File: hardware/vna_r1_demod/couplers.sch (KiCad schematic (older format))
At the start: 0 parts

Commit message: work on vna r1 demod schematic
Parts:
- added C? (x2): C_Small, symbol C_Small
- added R? (x2): R_Small, symbol R_Small
- added TP?: TP_RF, symbol TP_RF
- added U? (x2): resistive_bridge, symbol resistive_bridge
- added U? (x2): CONN_SMA_2GND, symbol CONN_SMA_2GND
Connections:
- new net GND: U?.4 (GND), U?.4 (GND)
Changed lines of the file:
@@
 $Descr A4 11693 8268
 encoding utf-8
-Sheet 1 4
+Sheet 5 6
 Title ""
 Date ""
@@
 Comment4 ""
 $EndDescr
+$Comp
+L resistive_bridge U?
+U 1 1 5AC73B65
+P 5150 4500
+F 0 "U?" H 4450 4900 60  0000 C CNN
+F 1 "resistive_bridge" H 4700 5000 60  0000 C CNN
+F 2 "" H 5450 4500 60  0001 C CNN
+F 3 "" H 5450 4500 60  0001 C CNN
+	1    5150 4500
+	1    0    0    -1
+$EndComp
+$Comp
+L resistive_bridge U?
+U 1 1 5AC73B7B
+P 7550 4500
+F 0 "U?" H 6850 4900 60  0000 C CNN
+F 1 "resistive_bridge" H 7100 5000 60  0000 C CNN
+F 2 "" H 7850 4500 60  0001 C CNN
+F 3 "" H 7850 4500 60  0001 C CNN
+	1    7550 4500
+	1    0    0    -1
+$EndComp
+$Comp
+L CONN_SMA_2GND U?
+U 1 1 5AC73BCD
+P 3000 4450
+F 0 "U?" H 2700 4650 60  0000 C CNN
+F 1 "CONN_SMA_2GND" H 3050 4750 60  0000 C CNN
+F 2 "" H 3000 4450 60  0000 C CNN
+F 3 "" H 3000 4450 60  0000 C CNN
+	1    3000 4450
+	1    0    0    -1
+$EndComp
+$Comp
+L CONN_SMA_2GND U?
+U 1 1 5AC73C3F
+P 9800 4450
+F 0 "U?" H 9500 4650 60  0000 C CNN
+F 1 "CONN_SMA_2GND" H 9850 4750 60  0000 C CNN
+F 2 "" H 9800 4450 60  0000 C CNN
+F 3 "" H 9800 4450 60  0000 C CNN
+	1    9800 4450
+	-1   0    0    -1
+$EndComp
+$Comp
+L R_Small R?
+U 1 1 5AC73CAD
+P 5100 3550
+F 0 "R?" H 5130 3570 50  0000 L CNN
+F 1 "R_Small" H 5130 3510 50  0000 L CNN
+F 2 "" H 5100 3550 50  0001 C CNN
+F 3 "" H 5100 3550 50  0001 C CNN
+	1    5100 3550
+	1    0    0    -1
+$EndComp
+$Comp
+L R_Small R?
+U 1 1 5AC73D0D
+P 7550 3500
+F 0 "R?" H 7580 3520 50  0000 L CNN
+F 1 "R_Small" H 7580 3460 50  0000 L CNN
+F 2 "" H 7550 3500 50  0001 C CNN
+F 3 "" H 7550 3500 50  0001 C CNN
+	1    7550 3500
+	1    0    0    -1
+$EndComp
+Text HLabel 5100 3050 1    60   Output ~ 0
+CPL_FWD
+Text HLabel 7900 3100 1    60   Output ~ 0
+CPL_REV
+$Comp
+L TP_RF TP?
+U 1 1 5AC74090
+P 6350 5000
+F 0 "TP?" V 6150 5150 60  0000 C CNN
+F 1 "TP_RF" V 6150 4900 60  0001 C CNN
+F 2 "" H 6350 5100 60  0001 C CNN
+F 3 "" H 6350 5100 60  0001 C CNN
+	1    6350 5000
+	1    0    0    -1
+$EndComp
+$Comp
+L GND #PWR?
+U 1 1 5AC74432
+P 5150 5050
+F 0 "#PWR?" H 5150 4800 50  0001 C CNN
+F 1 "GND" H 5150 4900 50  0000 C CNN
+F 2 "" H 5150 5050 50  0001 C CNN
+F 3 "" H 5150 5050 50  0001 C CNN
+	1    5150 5050
+	1    0    0    -1
+$EndComp
+Wire Wire Line
+	5150 4950 5150 5050
+$Comp
+L GND #PWR?
+U 1 1 5AC74470
+P 7550 5050
+F 0 "#PWR?" H 7550 4800 50  0001 C CNN
+F 1 "GND" H 7550 4900 50  0000 C CNN
+F 2 "" H 7550 5050 50  0001 C CNN
+F 3 "" H 7550 5050 50  0001 C CNN
+	1    7550 5050
+	1    0    0    -1
+$EndComp
+Wire Wire Line
+	7550 5050 7550 4950
+$Comp
+L C_Small C?
+U 1 1 5AC74707
+P 8900 4500
+F 0 "C?" H 8910 4570 50  0000 L CNN
+F 1 "C_Small" H 8910 4420 50  0000 L CNN
+F 2 "" H 8900 4500 50  0001 C CNN
+F 3 "" H 8900 4500 50  0001 C CNN
+	1    8900 4500
+	0    -1   -1   0
+$EndComp
+$Comp
+L C_Small C?
+U 1 1 5AC748D3
+P 3850 4500
+F 0 "C?" H 3860 4570 50  0000 L CNN
+F 1 "C_Small" H 3860 4420 50  0000 L CNN
+F 2 "" H 3850 4500 50  0001 C CNN
+F 3 "" H 3850 4500 50  0001 C CNN
+	1    3850 4500
+	0    -1   -1   0
+$EndComp
 $EndSCHEMATC

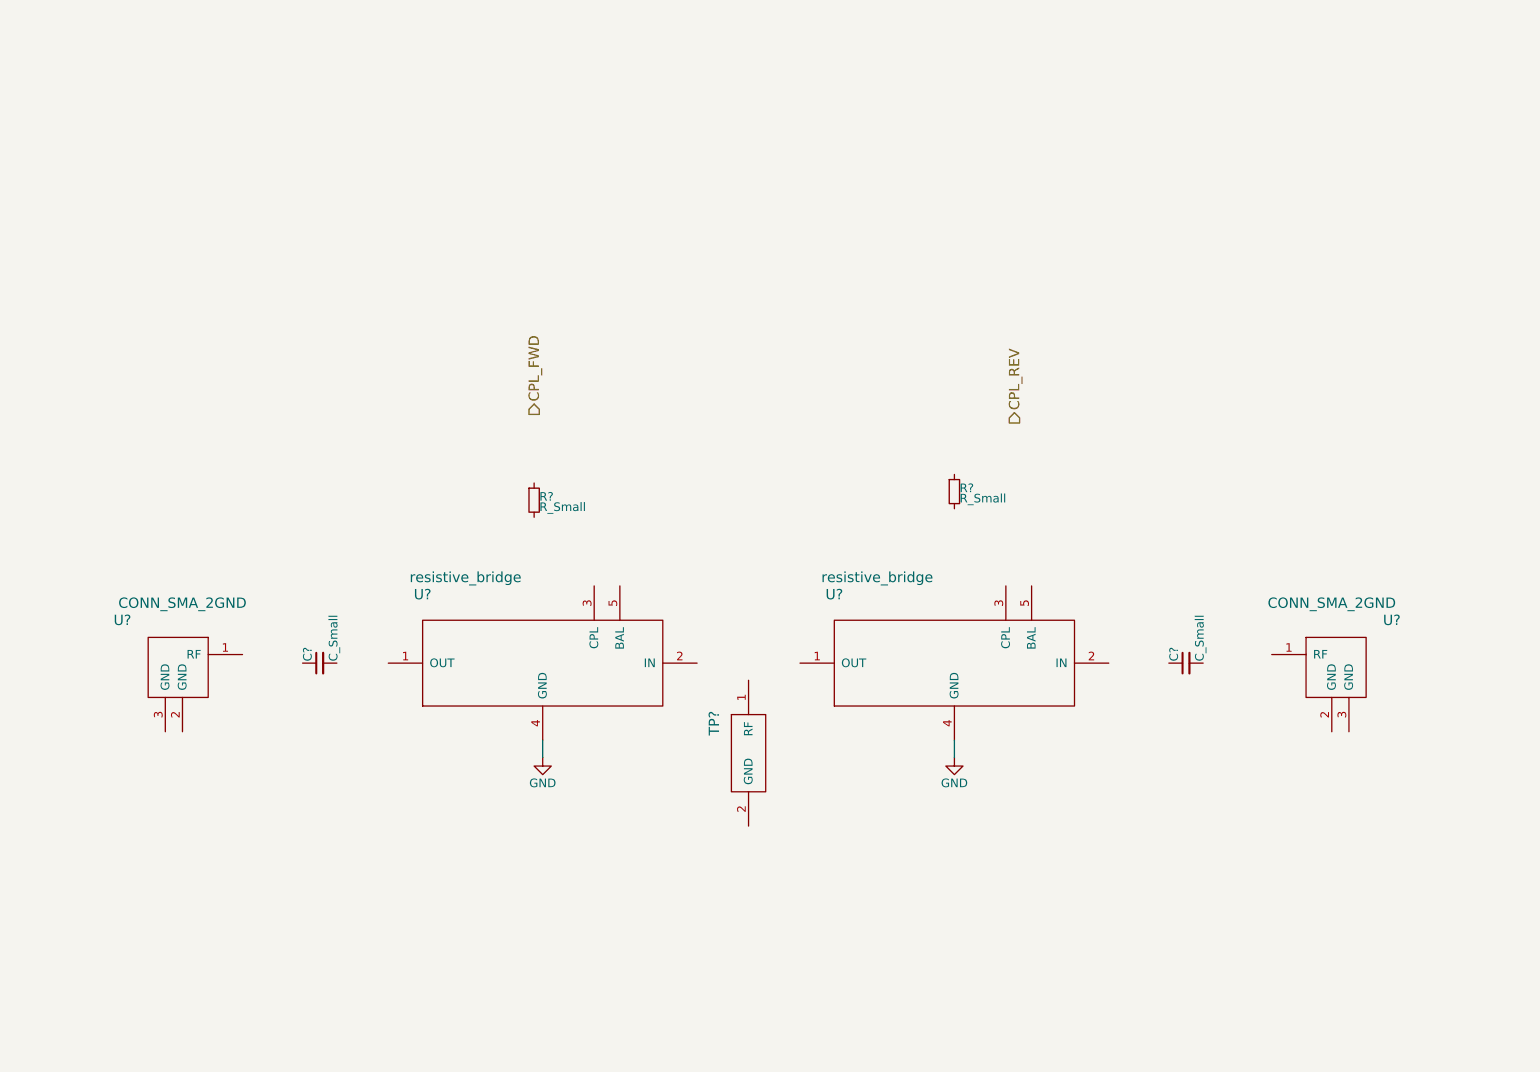
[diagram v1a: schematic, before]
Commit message: ethernet and usb layout on vna control board..
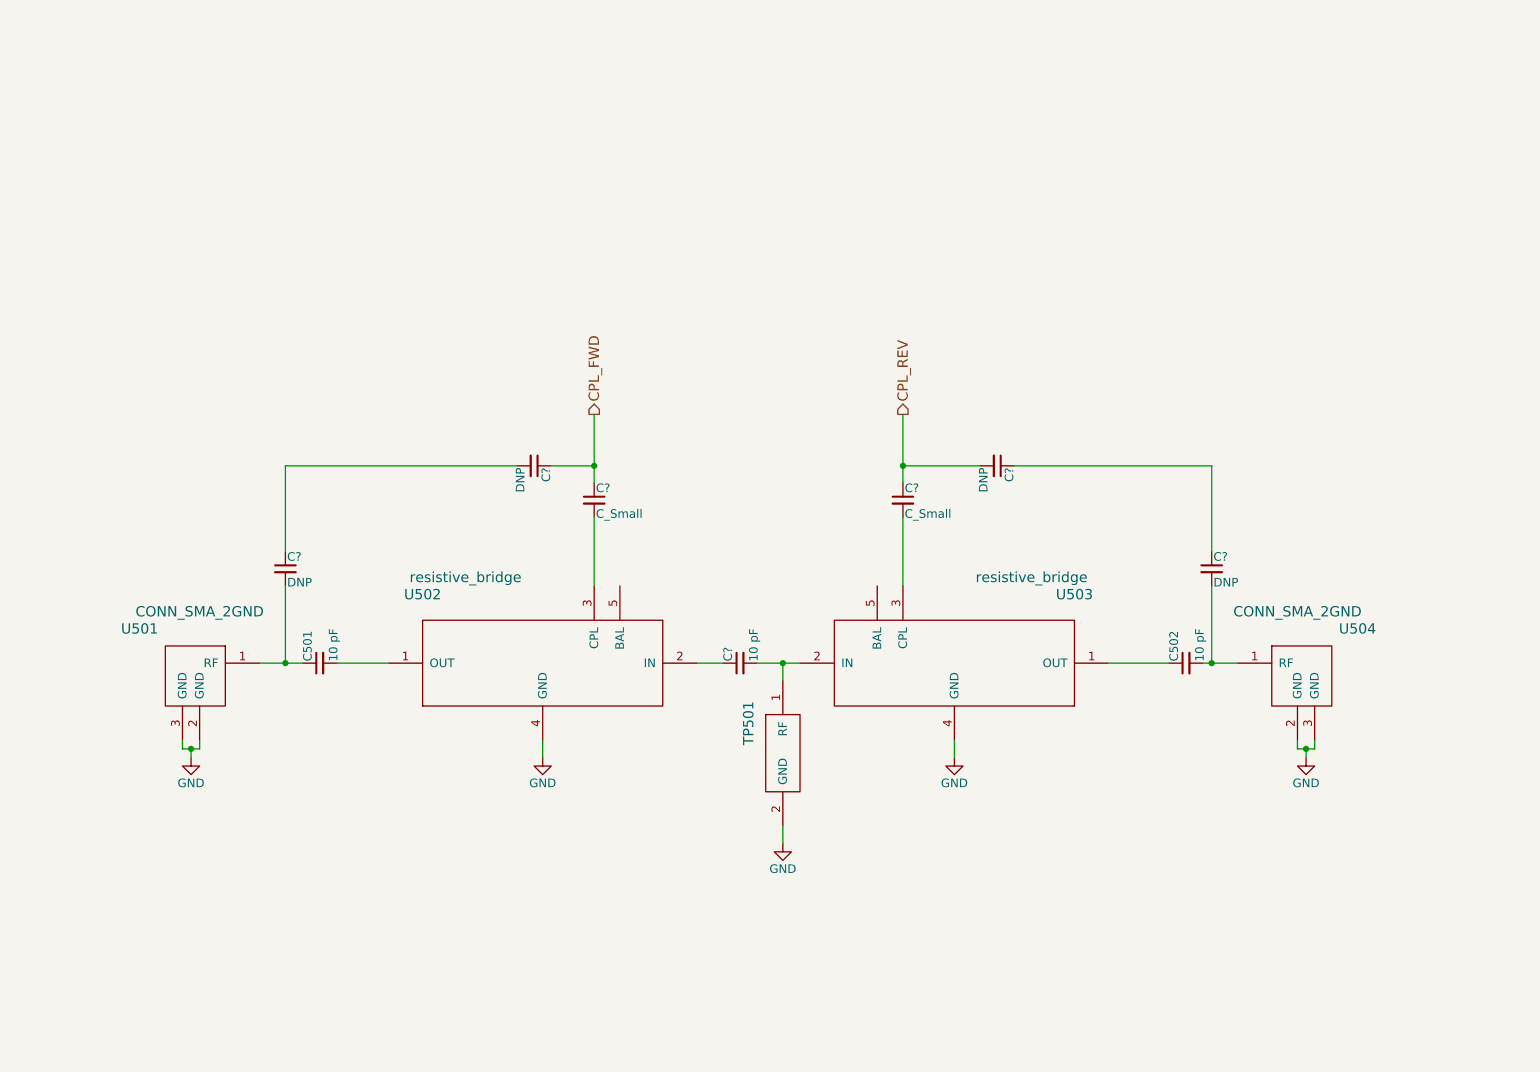
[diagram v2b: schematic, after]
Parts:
- removed R? (x2): R_Small, symbol R_Small
- added C?: 10 pF, symbol C_Small
- added C? (x4): DNP, symbol C_Small
- added C? (x2): C_Small, symbol C_Small
- C501, C502: renamed from C?; value C_Small -> 10 pF
- TP501: renamed from TP?; footprint (none) -> vna_footprints:TP-P20B
- U501, U504: renamed from U?; footprint (none) -> vna_footprints:SMA_901-10512_6p7MIL_FR408_CPW_LAUNCH
- U502, U503: renamed from U?; footprint (none) -> vna_footprints:resistive_bridge_osh_fr408_ustrip
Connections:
- net CPL_FWD: now also C?.1, C?.1
- net CPL_REV: now also C?.1, C?.2
- net GND: now also TP501.2 (GND), U501.2 (GND), U501.3 (GND), U504.2 (GND), U504.3 (GND)
- net at U502.1 (OUT): now also C501.2
- net at U502.2 (IN): now also C?.1
- net at U502.3 (CPL): now also C?.2
- net at U503.1 (OUT): now also C502.1
- net at U503.2 (IN): now also TP501.1 (RF), C?.2
- net at U503.3 (CPL): now also C?.2
- net at U501.1 (RF): now also C501.1, C?.2
- net at U504.1 (RF): now also C502.2, C?.2
- new net: C?.1, C?.2
- new net: C?.1, C?.1
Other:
- moved on the sheet: TP501, U501, U504

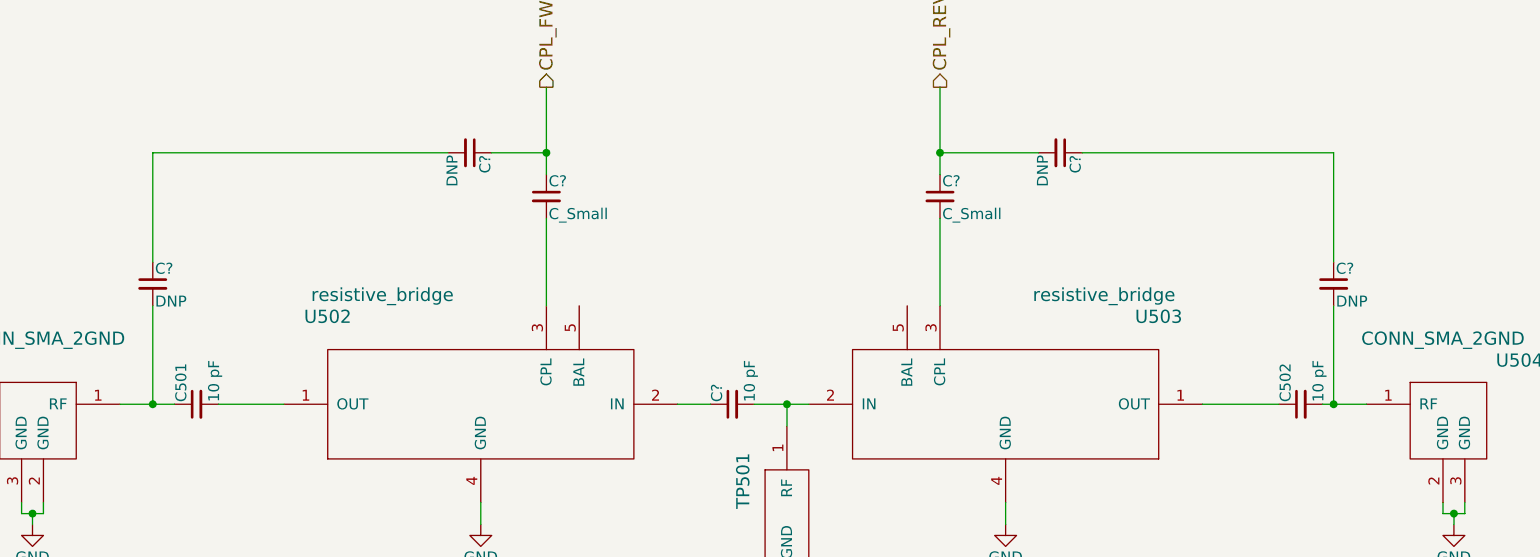
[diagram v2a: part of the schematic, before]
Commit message: footprint assignment for vna r1 synth and demod
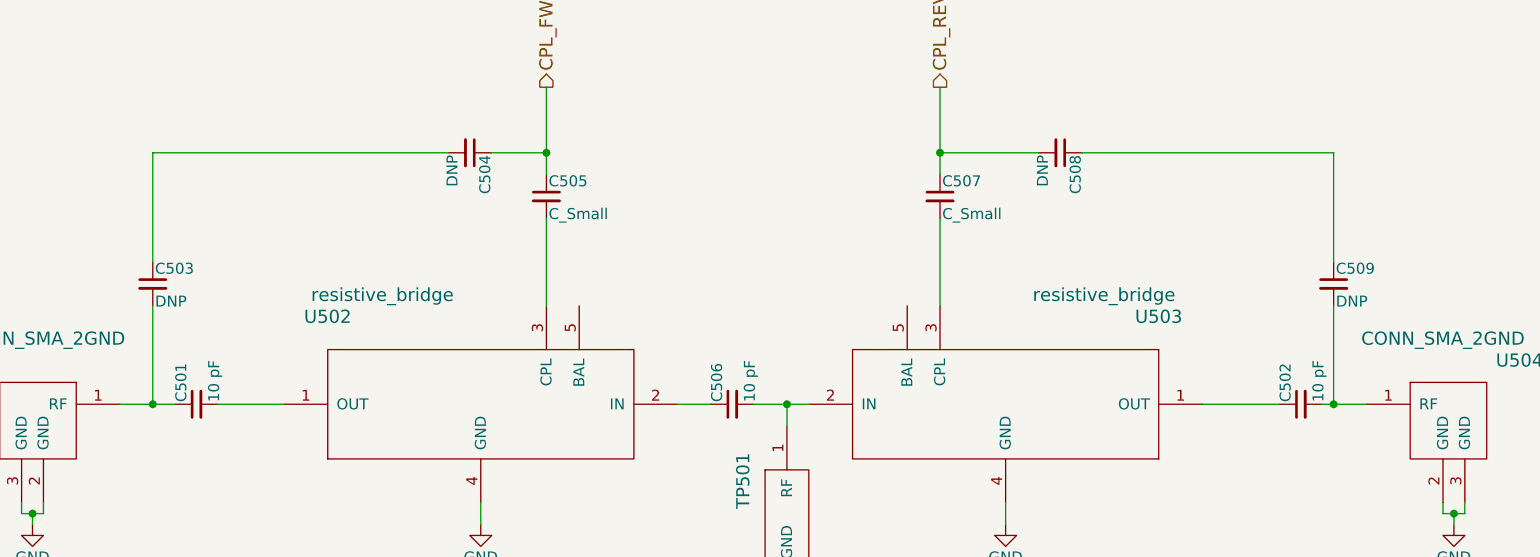
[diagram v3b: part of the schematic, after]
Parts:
- C501, C502: footprint (none) -> Capacitors_SMD:C_0201
- C503, C504, C505, C506, C507, C508, C509: renamed from C?; footprint (none) -> Capacitors_SMD:C_0201
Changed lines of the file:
@@
 $EndComp
 $Comp
-L GND #PWR070
+L GND #PWR502
 U 1 1 5AC74432
 P 5150 5050
-F 0 "#PWR070" H 5150 4800 50  0001 C CNN
+F 0 "#PWR502" H 5150 4800 50  0001 C CNN
 F 1 "GND" H 5150 4900 50  0000 C CNN
 F 2 "" H 5150 5050 50  0001 C CNN
@@
 $EndComp
 $Comp
-L GND #PWR071
+L GND #PWR504
 U 1 1 5AC74470
 P 7550 5050
-F 0 "#PWR071" H 7550 4800 50  0001 C CNN
+F 0 "#PWR504" H 7550 4800 50  0001 C CNN
 F 1 "GND" H 7550 4900 50  0000 C CNN
 F 2 "" H 7550 5050 50  0001 C CNN
@@
 F 0 "C502" H 8910 4570 50  0000 L CNN
 F 1 "10 pF" H 8910 4420 50  0000 L CNN
-F 2 "" H 8900 4500 50  0001 C CNN
+F 2 "Capacitors_SMD:C_0201" H 8900 4500 50  0001 C CNN
 F 3 "" H 8900 4500 50  0001 C CNN
 	1    8900 4500
@@
 F 0 "C501" H 3860 4570 50  0000 L CNN
 F 1 "10 pF" H 3860 4420 50  0000 L CNN
-F 2 "" H 3850 4500 50  0001 C CNN
+F 2 "Capacitors_SMD:C_0201" H 3850 4500 50  0001 C CNN
 F 3 "" H 3850 4500 50  0001 C CNN
 	1    3850 4500
@@
 $EndComp
 $Comp
-L C_Small C?
+L C_Small C506
 U 1 1 5AC9B899
 P 6300 4500
-F 0 "C?" H 6310 4570 50  0000 L CNN
+F 0 "C506" H 6310 4570 50  0000 L CNN
 F 1 "10 pF" H 6310 4420 50  0000 L CNN
-F 2 "" H 6300 4500 50  0001 C CNN
+F 2 "Capacitors_SMD:C_0201" H 6300 4500 50  0001 C CNN
 F 3 "" H 6300 4500 50  0001 C CNN
 	1    6300 4500
@@
 $EndComp
 $Comp
-L GND #PWR?
+L GND #PWR503
 U 1 1 5AC9BA0A
 P 6550 5550
-F 0 "#PWR?" H 6550 5300 50  0001 C CNN
+F 0 "#PWR503" H 6550 5300 50  0001 C CNN
 F 1 "GND" H 6550 5400 50  0000 C CNN
 F 2 "" H 6550 5550 50  0001 C CNN
@@
 $EndComp
 $Comp
-L GND #PWR?
+L GND #PWR505
 U 1 1 5AC9BE64
 P 9600 5050
-F 0 "#PWR?" H 9600 4800 50  0001 C CNN
+F 0 "#PWR505" H 9600 4800 50  0001 C CNN
 F 1 "GND" H 9600 4900 50  0000 C CNN
 F 2 "" H 9600 5050 50  0001 C CNN
@@
 $EndComp
 $Comp
-L GND #PWR?
+L GND #PWR501
 U 1 1 5AC9BF60
 P 3100 5050
-F 0 "#PWR?" H 3100 4800 50  0001 C CNN
+F 0 "#PWR501" H 3100 4800 50  0001 C CNN
 F 1 "GND" H 3100 4900 50  0000 C CNN
 F 2 "" H 3100 5050 50  0001 C CNN
@@
 $EndComp
 $Comp
-L C_Small C?
+L C_Small C503
 U 1 1 5AC9BE83
 P 3650 3950
-F 0 "C?" H 3660 4020 50  0000 L CNN
+F 0 "C503" H 3660 4020 50  0000 L CNN
 F 1 "DNP" H 3660 3870 50  0000 L CNN
-F 2 "" H 3650 3950 50  0001 C CNN
+F 2 "Capacitors_SMD:C_0201" H 3650 3950 50  0001 C CNN
 F 3 "" H 3650 3950 50  0001 C CNN
 	1    3650 3950
@@
 $EndComp
 $Comp
-L C_Small C?
+L C_Small C505
 U 1 1 5AC9D3B3
 P 5450 3550
-F 0 "C?" H 5460 3620 50  0000 L CNN
+F 0 "C505" H 5460 3620 50  0000 L CNN
 F 1 "C_Small" H 5460 3470 50  0000 L CNN
-F 2 "" H 5450 3550 50  0001 C CNN
+F 2 "Capacitors_SMD:C_0201" H 5450 3550 50  0001 C CNN
 F 3 "" H 5450 3550 50  0001 C CNN
 	1    5450 3550
@@
 $EndComp
 $Comp
-L C_Small C?
+L C_Small C507
 U 1 1 5AC9DC5E
 P 7250 3550
-F 0 "C?" H 7260 3620 50  0000 L CNN
+F 0 "C507" H 7260 3620 50  0000 L CNN
 F 1 "C_Small" H 7260 3470 50  0000 L CNN
-F 2 "" H 7250 3550 50  0001 C CNN
+F 2 "Capacitors_SMD:C_0201" H 7250 3550 50  0001 C CNN
 F 3 "" H 7250 3550 50  0001 C CNN
 	1    7250 3550
@@
 $EndComp
 $Comp
-L C_Small C?
+L C_Small C509
 U 1 1 5AC9DD2F
 P 9050 3950
-F 0 "C?" H 9060 4020 50  0000 L CNN
+F 0 "C509" H 9060 4020 50  0000 L CNN
 F 1 "DNP" H 9060 3870 50  0000 L CNN
-F 2 "" H 9050 3950 50  0001 C CNN
+F 2 "Capacitors_SMD:C_0201" H 9050 3950 50  0001 C CNN
 F 3 "" H 9050 3950 50  0001 C CNN
 	1    9050 3950
@@
 $EndComp
 $Comp
-L C_Small C?
+L C_Small C504
 U 1 1 5AC9EAD5
 P 5100 3350
-F 0 "C?" H 5110 3420 50  0000 L CNN
+F 0 "C504" H 5110 3420 50  0000 L CNN
 F 1 "DNP" H 5110 3270 50  0000 L CNN
-F 2 "" H 5100 3350 50  0001 C CNN
+F 2 "Capacitors_SMD:C_0201" H 5100 3350 50  0001 C CNN
 F 3 "" H 5100 3350 50  0001 C CNN
 	1    5100 3350
@@
 	3650 3350 5000 3350
 $Comp
-L C_Small C?
+L C_Small C508
 U 1 1 5AC9EC4A
 P 7800 3350
-F 0 "C?" H 7810 3420 50  0000 L CNN
+F 0 "C508" H 7810 3420 50  0000 L CNN
 F 1 "DNP" H 7810 3270 50  0000 L CNN
-F 2 "" H 7800 3350 50  0001 C CNN
+F 2 "Capacitors_SMD:C_0201" H 7800 3350 50  0001 C CNN
 F 3 "" H 7800 3350 50  0001 C CNN
 	1    7800 3350
